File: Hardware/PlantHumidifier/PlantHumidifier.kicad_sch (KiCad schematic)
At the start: 8 parts, among them J1 110990030, J2 Conn_01x05_Female, J3 Conn_01x04_Female, J4 Conn_01x04_Female, U1 WeMos_D1_mini

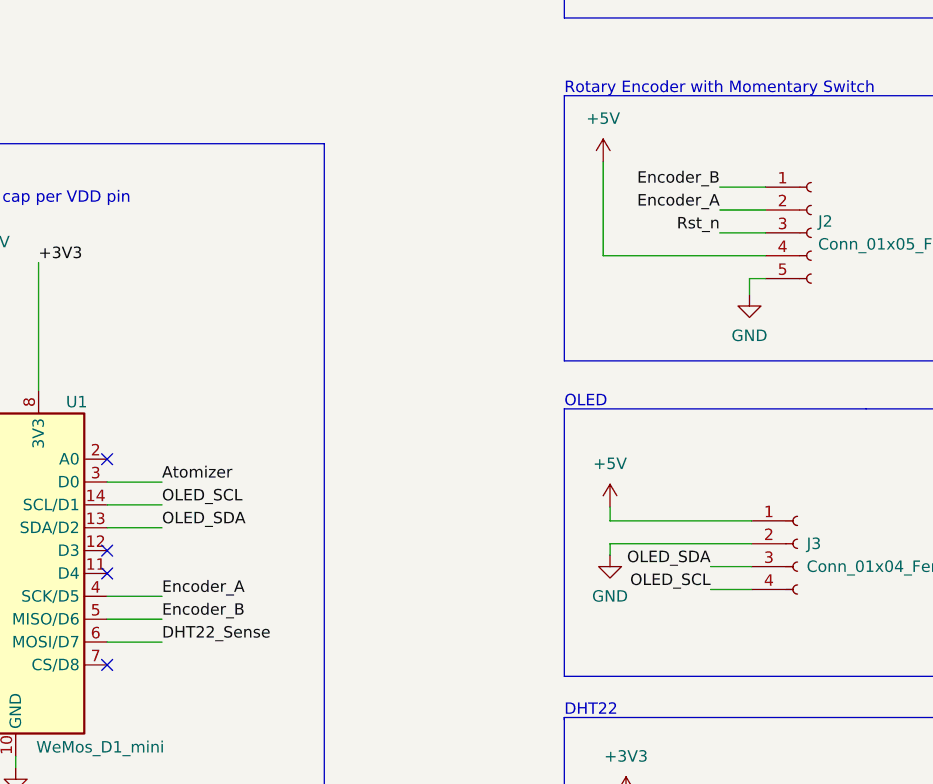
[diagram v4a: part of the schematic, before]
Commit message: Update pins again for easier routing (reflected in layout + schematic here as well)
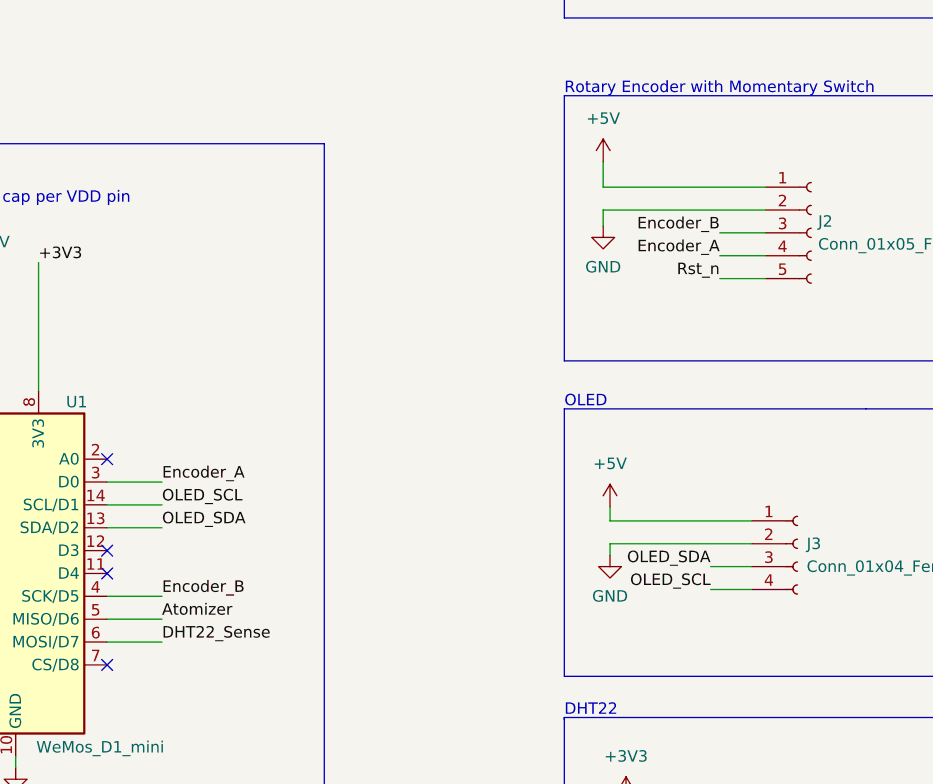
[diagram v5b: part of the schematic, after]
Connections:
- net +5V: now also J2.1 (Pin_1); no longer J2.4 (Pin_4)
- net Atomizer: now also U1.5 (MISO/D6); no longer U1.3 (D0)
- net Encoder_A: now also J2.4 (Pin_4), U1.3 (D0); no longer J2.2 (Pin_2), U1.4 (SCK/D5)
- net Encoder_B: now also J2.3 (Pin_3), U1.4 (SCK/D5); no longer J2.1 (Pin_1), U1.5 (MISO/D6)
- net GND: now also J2.2 (Pin_2); no longer J2.5 (Pin_5)
- net Rst_n: now also J2.5 (Pin_5); no longer J2.3 (Pin_3)

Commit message: Schematic: Add mounting holes (Size M2)
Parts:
- added H? (x4): MountingHole, MountingHole:MountingHole_2.2mm_M2, symbol Mechanical:MountingHole
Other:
- note added: "Mounting Holes"
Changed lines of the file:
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@@
+    (stroke (width 0) (type default) (color 0 0 0 0))
+  )
+  (polyline (pts (xy 37.846 85.852) (xy 57.912 85.852))
     (stroke (width 0) (type default) (color 0 0 0 0))
   )
@@
     (stroke (width 0) (type default) (color 0 0 0 0))
   )
+  (polyline (pts (xy 57.912 85.852) (xy 57.912 110.236))
+    (stroke (width 0) (type default) (color 0 0 0 0))
+  )
   (polyline (pts (xy 176.276 124.46) (xy 176.276 162.306))
     (stroke (width 0) (type default) (color 0 0 0 0))
   )
+  (polyline (pts (xy 57.912 110.236) (xy 37.592 110.236))
+    (stroke (width 0) (type default) (color 0 0 0 0))
+  )
   (polyline (pts (xy 222.758 19.05) (xy 176.276 19.05))
     (stroke (width 0) (type default) (color 0 0 0 0))
@@
     (stroke (width 0) (type default) (color 0 0 0 0))
   )
+  (polyline (pts (xy 37.592 110.236) (xy 37.592 85.852))
+    (stroke (width 0) (type default) (color 0 0 0 0))
+  )
   (wire (pts (xy 207.01 142.24) (xy 212.344 142.24))
     (stroke (width 0) (type default) (color 0 0 0 0))
@@
   )
   (text "Power" (at 37.338 57.404 0)
+    (effects (font (size 1.27 1.27)) (justify left bottom))
+  )
+  (text "Mounting Holes" (at 37.846 85.852 0)
     (effects (font (size 1.27 1.27)) (justify left bottom))
   )
@@
   (label "Encoder_B" (at 131.572 110.998 0)
     (effects (font (size 1.27 1.27)) (justify left bottom))
+  )
+  (symbol (lib_id "Mechanical:MountingHole") (at 40.894 100.838 180) (unit 1)
+    (in_bom yes) (on_board yes) (fields_autoplaced)
+    (property "Reference" "H?" (id 0) (at 43.688 99.5679 0)
+      (effects (font (size 1.27 1.27)) (justify right))
+    )
+    (property "Value" "MountingHole" (id 1) (at 43.688 102.1079 0)
+      (effects (font (size 1.27 1.27)) (justify right))
+    )
+    (property "Footprint" "MountingHole:MountingHole_2.2mm_M2" (id 2) (at 40.894 100.838 0)
+      (effects (font (size 1.27 1.27)) hide)
+    )
+    (property "Datasheet" "~" (id 3) (at 40.894 100.838 0)
+      (effects (font (size 1.27 1.27)) hide)
+    )
   )
   (symbol (lib_id "Device:C") (at 100.838 82.042 0) (unit 1)
@@
     (pin "4")
   )
+  (symbol (lib_id "Mechanical:MountingHole") (at 40.894 90.678 180) (unit 1)
+    (in_bom yes) (on_board yes) (fields_autoplaced)
+    (property "Reference" "H?" (id 0) (at 43.688 89.4079 0)
+      (effects (font (size 1.27 1.27)) (justify right))
+    )
+    (property "Value" "MountingHole" (id 1) (at 43.688 91.9479 0)
+      (effects (font (size 1.27 1.27)) (justify right))
+    )
+    (property "Footprint" "MountingHole:MountingHole_2.2mm_M2" (id 2) (at 40.894 90.678 0)
+      (effects (font (size 1.27 1.27)) hide)
+    )
+    (property "Datasheet" "~" (id 3) (at 40.894 90.678 0)
+      (effects (font (size 1.27 1.27)) hide)
+    )
+  )
   (symbol (lib_id "power:+5V") (at 112.776 76.454 0) (unit 1)
     (in_bom yes) (on_board yes) (fields_autoplaced)
@@
     )
     (pin "1")
+  )
+  (symbol (lib_id "Mechanical:MountingHole") (at 40.894 95.758 180) (unit 1)
+    (in_bom yes) (on_board yes) (fields_autoplaced)
+    (property "Reference" "H?" (id 0) (at 43.688 94.4879 0)
+      (effects (font (size 1.27 1.27)) (justify right))
+    )
+    (property "Value" "MountingHole" (id 1) (at 43.688 97.0279 0)
+      (effects (font (size 1.27 1.27)) (justify right))
+    )
+    (property "Footprint" "MountingHole:MountingHole_2.2mm_M2" (id 2) (at 40.894 95.758 0)
+      (effects (font (size 1.27 1.27)) hide)
+    )
+    (property "Datasheet" "~" (id 3) (at 40.894 95.758 0)
+      (effects (font (size 1.27 1.27)) hide)
+    )
   )
   (symbol (lib_id "Connector:Conn_01x04_Female") (at 220.218 144.78 0) (unit 1)
@@
     )
     (pin "1")
+  )
+  (symbol (lib_id "Mechanical:MountingHole") (at 40.894 105.918 180) (unit 1)
+    (in_bom yes) (on_board yes) (fields_autoplaced)
+    (property "Reference" "H?" (id 0) (at 43.688 104.6479 0)
+      (effects (font (size 1.27 1.27)) (justify right))
+    )
+    (property "Value" "MountingHole" (id 1) (at 43.688 107.1879 0)
+      (effects (font (size 1.27 1.27)) (justify right))
+    )
+    (property "Footprint" "MountingHole:MountingHole_2.2mm_M2" (id 2) (at 40.894 105.918 0)
+      (effects (font (size 1.27 1.27)) hide)
+    )
+    (property "Datasheet" "~" (id 3) (at 40.894 105.918 0)
+      (effects (font (size 1.27 1.27)) hide)
+    )
   )
   (symbol (lib_id "power:GND") (at 115.316 130.048 0) (unit 1)
@@
       (reference "C2") (unit 1) (value "100n") (footprint "Capacitor_SMD:C_0402_1005Metric")
     )
+    (path "/037cd9e2-c436-45ce-9701-802b6fe49823"
+      (reference "H?") (unit 1) (value "MountingHole") (footprint "MountingHole:MountingHole_2.2mm_M2")
+    )
+    (path "/86be4c77-a4f0-44de-87ea-a4911c4bffb9"
+      (reference "H?") (unit 1) (value "MountingHole") (footprint "MountingHole:MountingHole_2.2mm_M2")
+    )
+    (path "/93a7b237-e301-4fc9-93dd-d06c3a220b65"
+      (reference "H?") (unit 1) (value "MountingHole") (footprint "MountingHole:MountingHole_2.2mm_M2")
+    )
+    (path "/f2af4d8a-cfbc-4b49-99cf-2715ce367108"
+      (reference "H?") (unit 1) (value "MountingHole") (footprint "MountingHole:MountingHole_2.2mm_M2")
+    )
     (path "/f617cd1b-909f-4cbb-bc4d-a14076c52ab4"

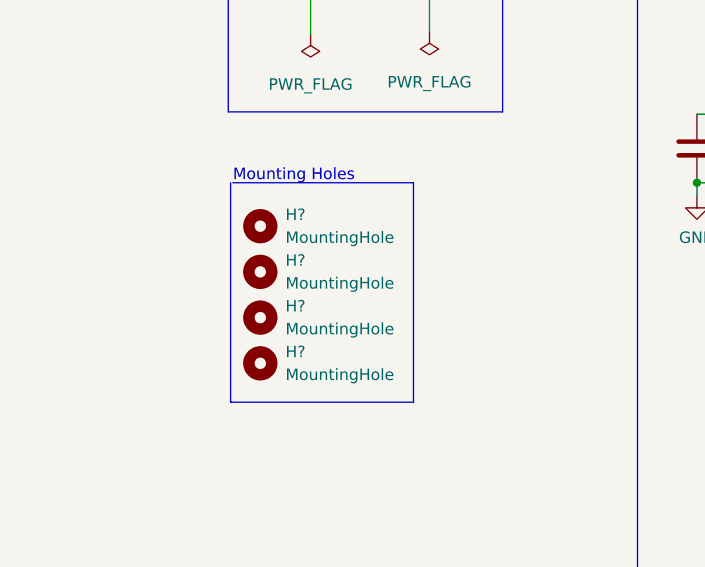
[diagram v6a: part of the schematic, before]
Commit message: Schematic: Update annotations
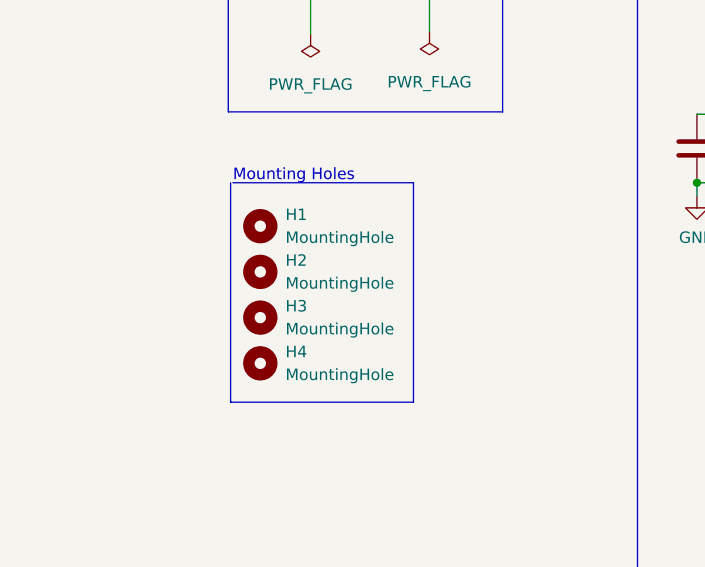
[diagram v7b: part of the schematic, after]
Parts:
- gave numbers to parts that had none: 4
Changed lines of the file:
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@@
   (symbol (lib_id "Mechanical:MountingHole") (at 40.894 100.838 180) (unit 1)
     (in_bom yes) (on_board yes) (fields_autoplaced)
-    (property "Reference" "H?" (id 0) (at 43.688 99.5679 0)
+    (property "Reference" "H3" (id 0) (at 43.688 99.5679 0)
       (effects (font (size 1.27 1.27)) (justify right))
     )
@@
   (symbol (lib_id "Mechanical:MountingHole") (at 40.894 90.678 180) (unit 1)
     (in_bom yes) (on_board yes) (fields_autoplaced)
-    (property "Reference" "H?" (id 0) (at 43.688 89.4079 0)
+    (property "Reference" "H1" (id 0) (at 43.688 89.4079 0)
       (effects (font (size 1.27 1.27)) (justify right))
     )
@@
   (symbol (lib_id "Mechanical:MountingHole") (at 40.894 95.758 180) (unit 1)
     (in_bom yes) (on_board yes) (fields_autoplaced)
-    (property "Reference" "H?" (id 0) (at 43.688 94.4879 0)
+    (property "Reference" "H2" (id 0) (at 43.688 94.4879 0)
       (effects (font (size 1.27 1.27)) (justify right))
     )
@@
   (symbol (lib_id "Mechanical:MountingHole") (at 40.894 105.918 180) (unit 1)
     (in_bom yes) (on_board yes) (fields_autoplaced)
-    (property "Reference" "H?" (id 0) (at 43.688 104.6479 0)
+    (property "Reference" "H4" (id 0) (at 43.688 104.6479 0)
       (effects (font (size 1.27 1.27)) (justify right))
     )
@@
       (reference "C2") (unit 1) (value "100n") (footprint "Capacitor_SMD:C_0402_1005Metric")
     )
+    (path "/86be4c77-a4f0-44de-87ea-a4911c4bffb9"
+      (reference "H1") (unit 1) (value "MountingHole") (footprint "MountingHole:MountingHole_2.2mm_M2")
+    )
+    (path "/93a7b237-e301-4fc9-93dd-d06c3a220b65"
+      (reference "H2") (unit 1) (value "MountingHole") (footprint "MountingHole:MountingHole_2.2mm_M2")
+    )
     (path "/037cd9e2-c436-45ce-9701-802b6fe49823"
-      (reference "H?") (unit 1) (value "MountingHole") (footprint "MountingHole:MountingHole_2.2mm_M2")
-    )
-    (path "/86be4c77-a4f0-44de-87ea-a4911c4bffb9"
-      (reference "H?") (unit 1) (value "MountingHole") (footprint "MountingHole:MountingHole_2.2mm_M2")
-    )
-    (path "/93a7b237-e301-4fc9-93dd-d06c3a220b65"
-      (reference "H?") (unit 1) (value "MountingHole") (footprint "MountingHole:MountingHole_2.2mm_M2")
+      (reference "H3") (unit 1) (value "MountingHole") (footprint "MountingHole:MountingHole_2.2mm_M2")
     )
     (path "/f2af4d8a-cfbc-4b49-99cf-2715ce367108"
-      (reference "H?") (unit 1) (value "MountingHole") (footprint "MountingHole:MountingHole_2.2mm_M2")
+      (reference "H4") (unit 1) (value "MountingHole") (footprint "MountingHole:MountingHole_2.2mm_M2")
     )
     (path "/f617cd1b-909f-4cbb-bc4d-a14076c52ab4"
